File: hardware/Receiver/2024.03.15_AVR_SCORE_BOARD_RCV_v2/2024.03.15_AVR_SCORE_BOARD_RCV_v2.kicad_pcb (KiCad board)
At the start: 2 copper layers, 41 parts, among them J1 ARK_01x03, J3 UART, J4 Conn_01x03, J5 Conn_01x03, J6 Conn_01x03, U1 ATmega328P-PU, U2 AIMTEC_AMSROL-78NZ, U3 NRF24l04, U4 PCF8563T, U5 LM1117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

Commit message: changed wrong footprints
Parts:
- added C13: 100nF, Capacitor_SMD:C_0805_2012Metric_Pad1.15x1.40mm_HandSolder, B.Cu at (54.7, 35.6)
- Y1: footprint Crystal:Crystal_HC52-6mm_Vertical -> Crystal:Crystal_HC49-U_Vertical
- moved Y1 0.71 mm to (52.5, 61.8)
- moved C2 0.11 mm to (52.6, 51.2), turned to 180 degrees
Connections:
- J3 pad 1: RST -> Net-(C13-Pad1)
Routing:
- net Net-(C8-Pad2): track 20.8 -> 12.8 mm
- net RST: track 82.1 -> 77.4 mm
- net +5V: track 248.1 -> 251.4 mm
- net Net-(C7-Pad2): track 18.1 -> 14.8 mm
- net GND: track 54.7 -> 57.4 mm
- net Net-(C13-Pad1): track 0.00 -> 1.60 mm

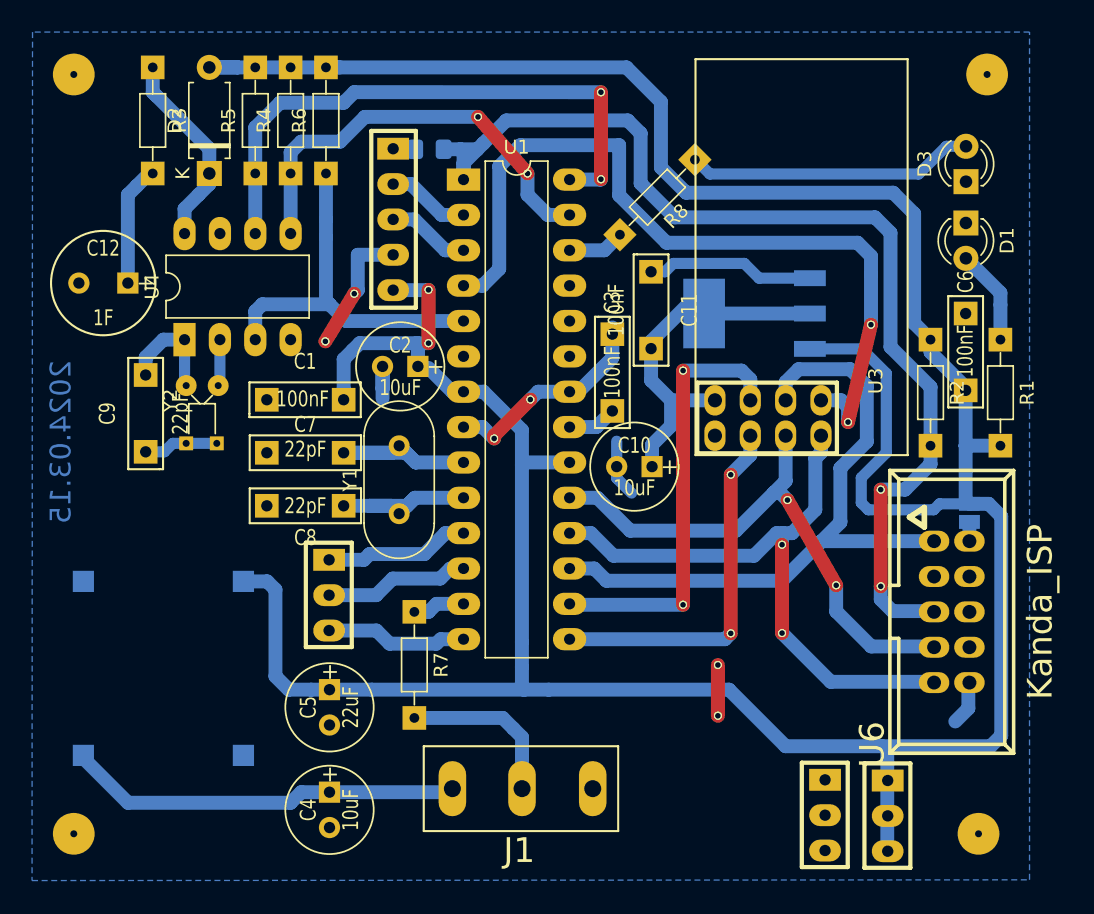
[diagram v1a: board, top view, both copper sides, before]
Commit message: Added 100nF capacitor for rtc
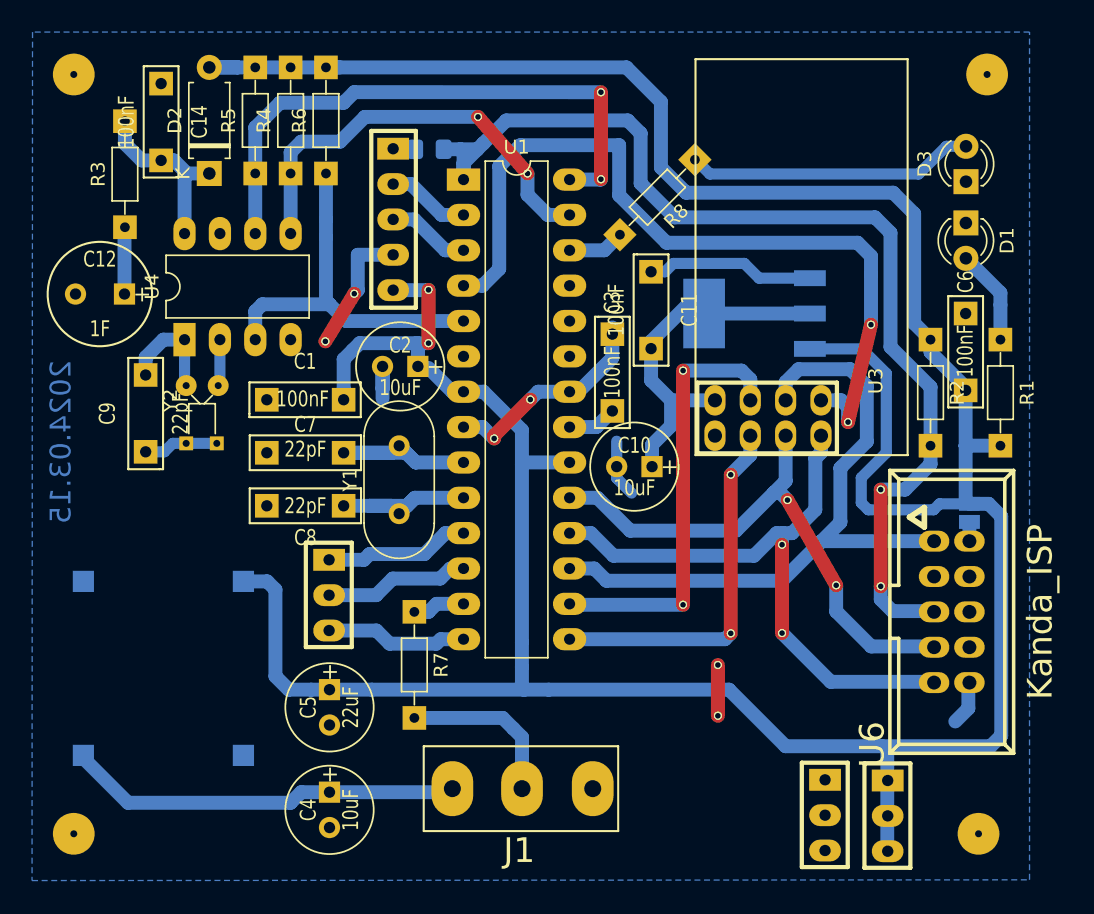
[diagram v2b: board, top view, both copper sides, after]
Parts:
- added C14: 100nF, Moje:C[5,5mm], F.Cu at (35.4, 33.6)
- moved R3 11.7 mm to (32.8, 41.2), turned to 90 degrees
- moved C12 0.82 mm to (31.0, 46.0)
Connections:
- D2 pad 1: Net-(D2-Pad1) -> Net-(C14-Pad1)
- R3 pad 1: Net-(D2-Pad1) -> Net-(C12-Pad1)
- R3 pad 2: Net-(C12-Pad1) -> Net-(C14-Pad1)
- U4 pad 8: Net-(D2-Pad1) -> Net-(C14-Pad1)
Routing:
- net Net-(D2-Pad1): track 14.9 -> 0.00 mm
- net Net-(C14-Pad1): track 0.00 -> 13.0 mm
- net Net-(C12-Pad1): track 9.02 -> 4.81 mm

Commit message: Added v2 version of TX schematic and pcb
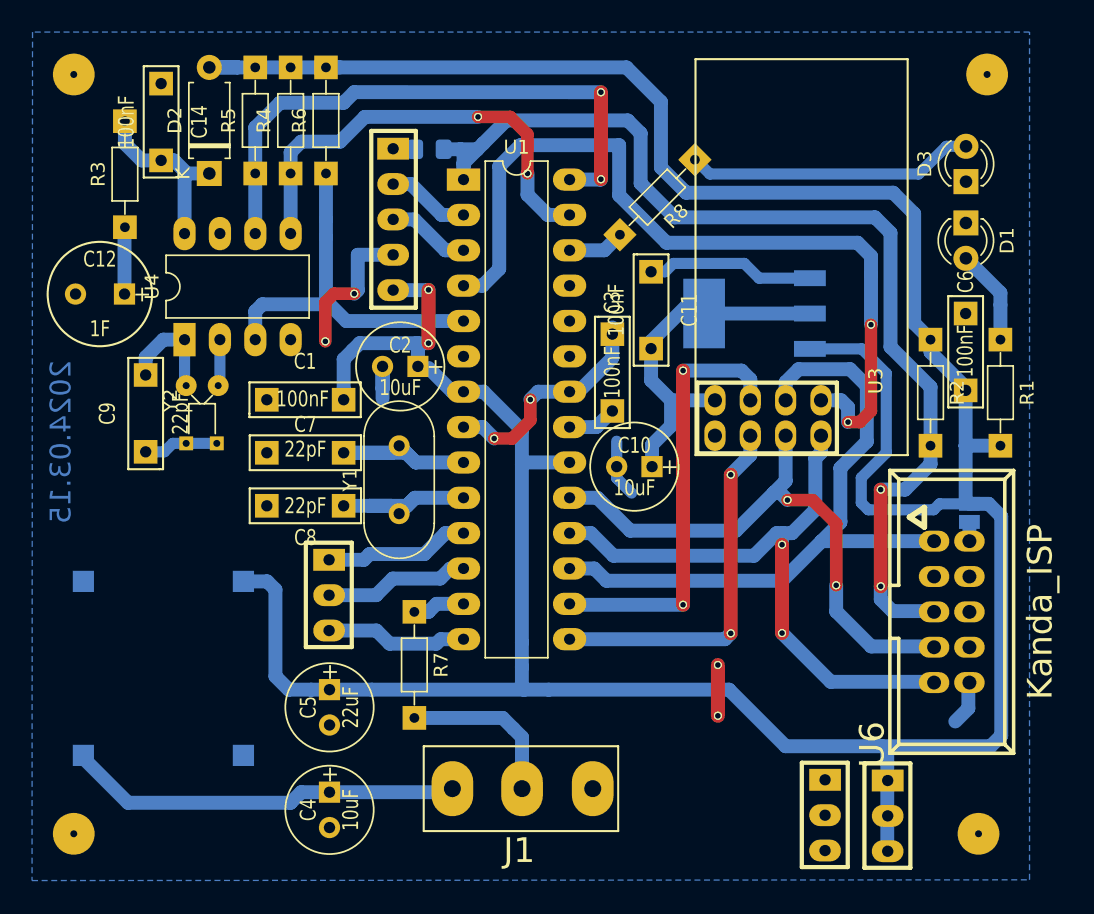
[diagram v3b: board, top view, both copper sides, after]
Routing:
- net GND: track 57.4 -> 59.3 mm
- net SCK: track 39.4 -> 40.9 mm
- net SDA: track 31.4 -> 32.9 mm
- net INT0_NRF: track 58.5 -> 59.5 mm

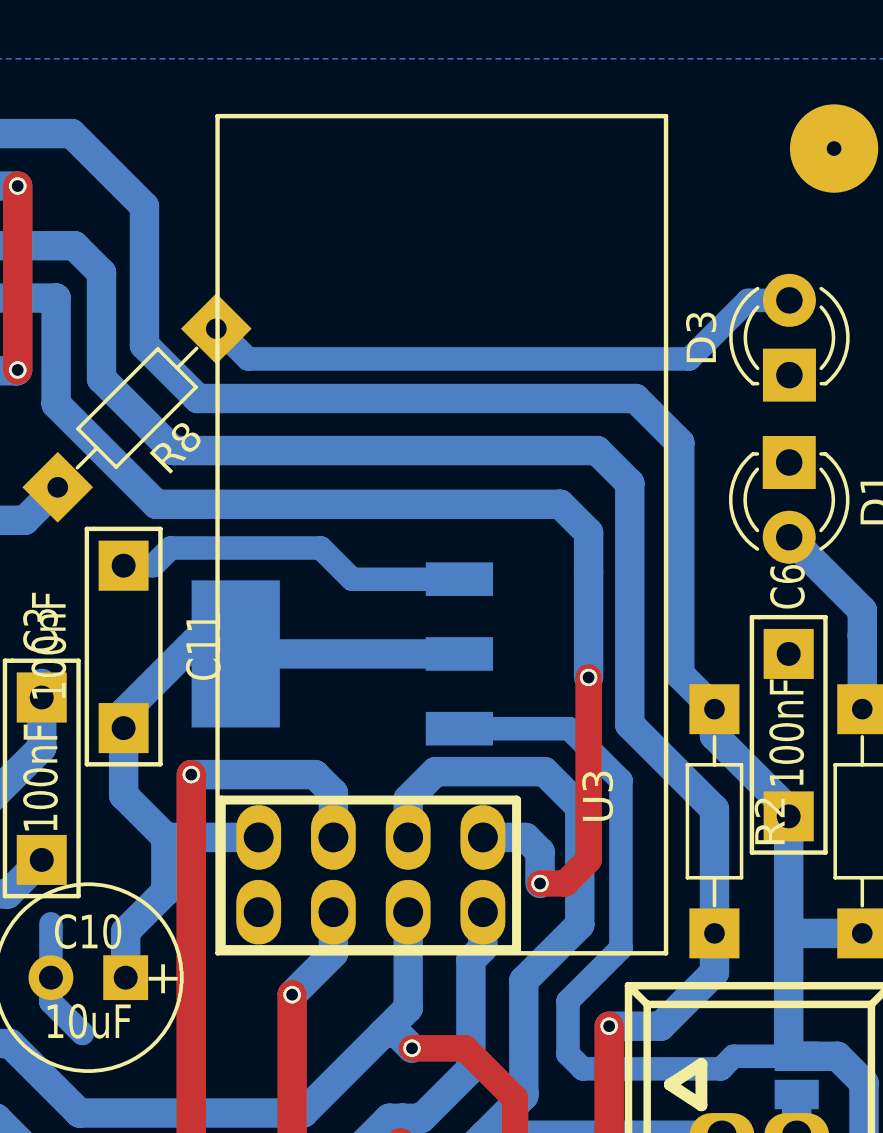
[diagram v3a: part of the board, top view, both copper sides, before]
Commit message: Fixed NRF24L01 schematic symbol
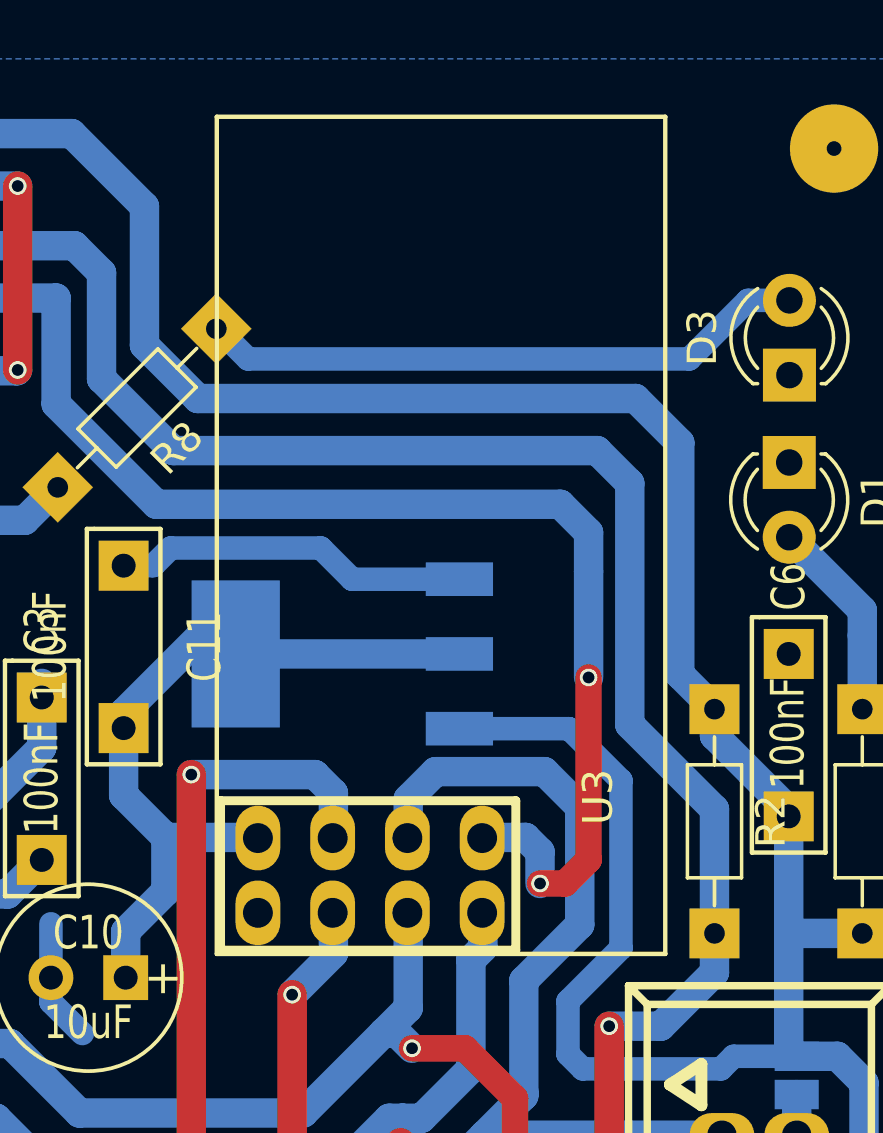
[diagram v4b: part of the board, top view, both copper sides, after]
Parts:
- U3: value NRF24l04 -> NRF24l01

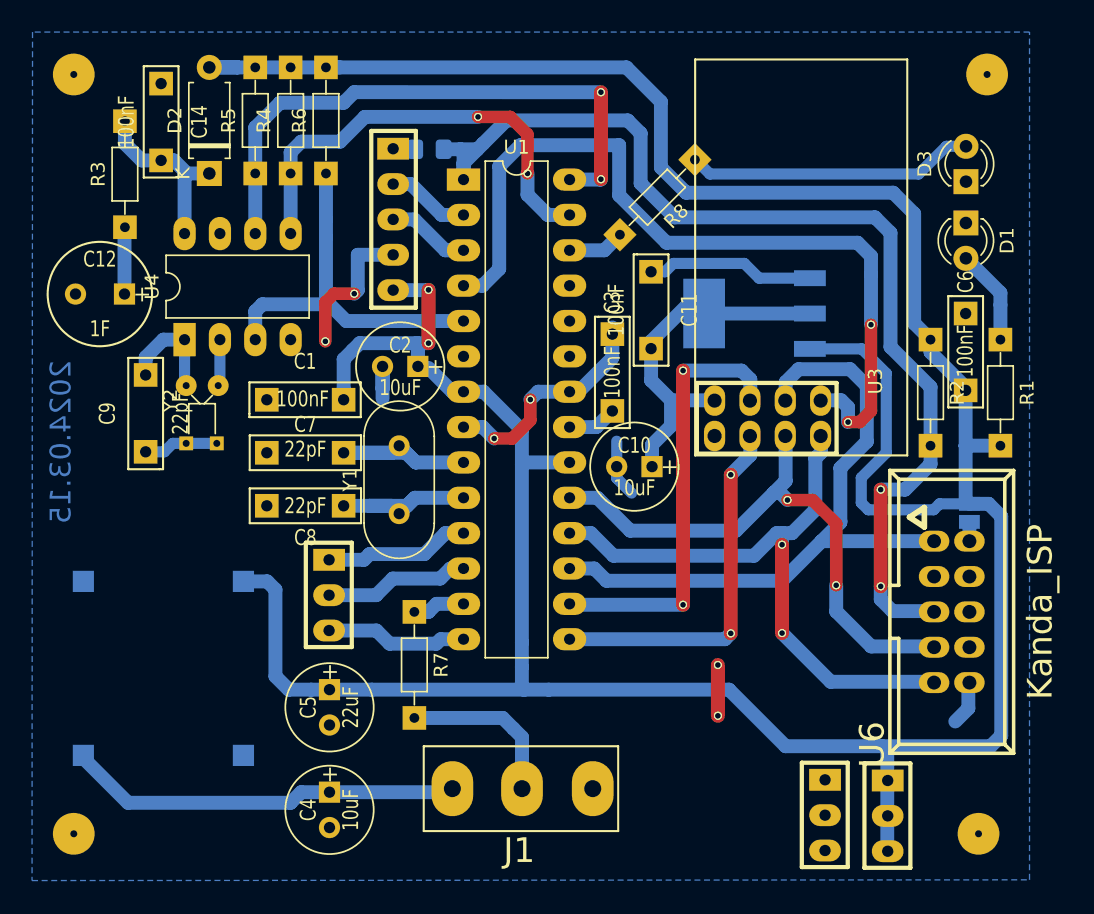
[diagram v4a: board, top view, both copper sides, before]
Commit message: RCV Hardware updated - Voltage regulation
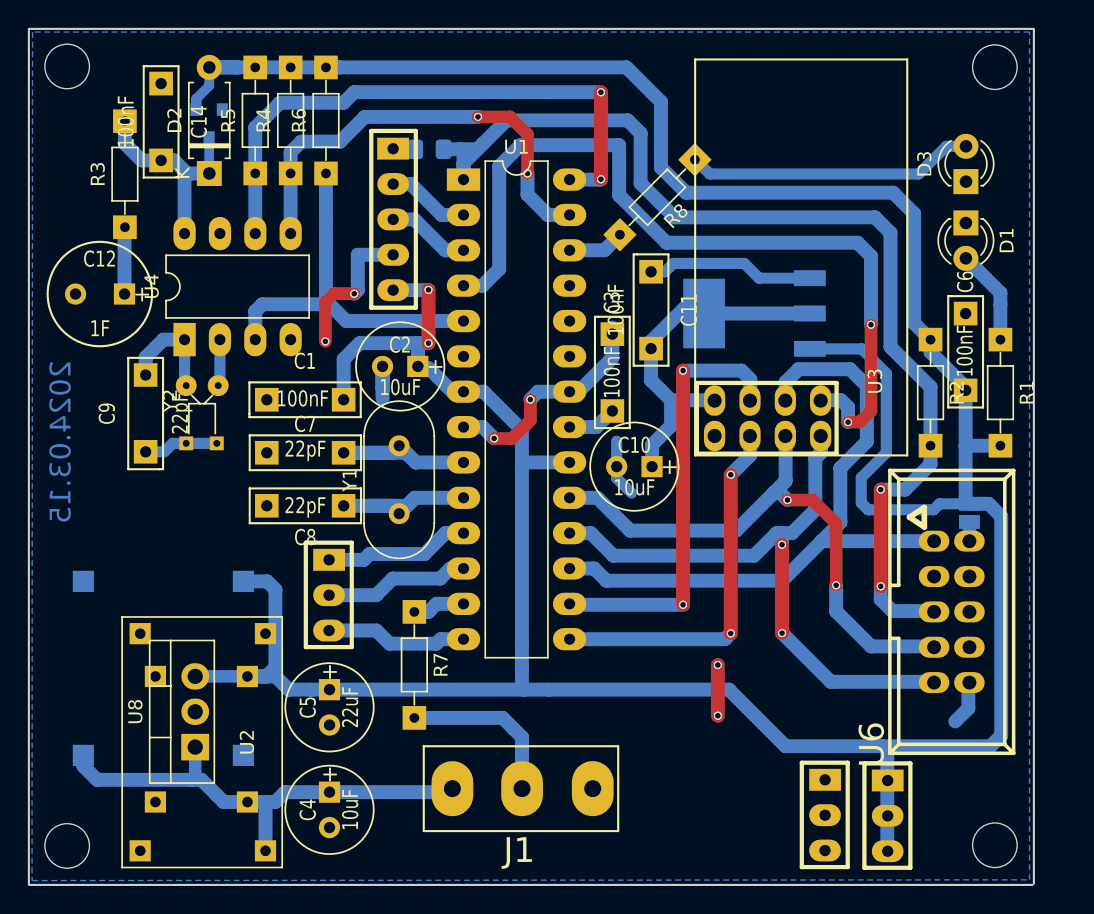
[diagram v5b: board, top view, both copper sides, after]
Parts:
- added D4: BAT54C, Package_TO_SOT_SMD:SOT-23, B.Cu at (38.9, 33.8)
- added U2: MH-MINI-360, Moje:MH-MINI_DC_DC, F.Cu at (38.3, 78.2)
- added U8: LM7805_TO220, Package_TO_SOT_THT:TO-220-3_Vertical, F.Cu at (37.9, 78.5)
- D2: value D_Schottky -> BA159
- H1, H2, H3, H4: footprint Moje:MountingHole_3mm -> MountingHole:MountingHole_3.2mm_M3
- moved H2 86.3 mm to (28.6, 85.7)
- moved H3 66.2 mm to (95.3, 85.6)
- moved H4 55.1 mm to (95.3, 29.7)
- moved H1 0.75 mm to (28.6, 29.6)
- renumbered U2 to U7
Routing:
- net +5V: track 251.4 -> 264.6 mm
- net +12V: track 28.4 -> 35.3 mm
- net Net-(C14-Pad1): track 13.0 -> 15.6 mm
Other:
- board outline added: 72.2 x 61.5 mm
